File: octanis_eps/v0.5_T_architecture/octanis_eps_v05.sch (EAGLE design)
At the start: 141 parts, among them IC1 OPA2333DGK, Q1 32.768kHz, Q100 BSS123, U1 CSD16327Q3_DQG_8, U10 CSD16327Q3_DQG_8, U100 Value, U11 CSD16327Q3_DQG_8, U2 CSD16327Q3_DQG_8, U3 CSD16327Q3_DQG_8, U4 MSP430G2544, U5 TPS2022D, U6 Value, U7 Value, U8 TPS61232, U9 BQ24650_RVA_16

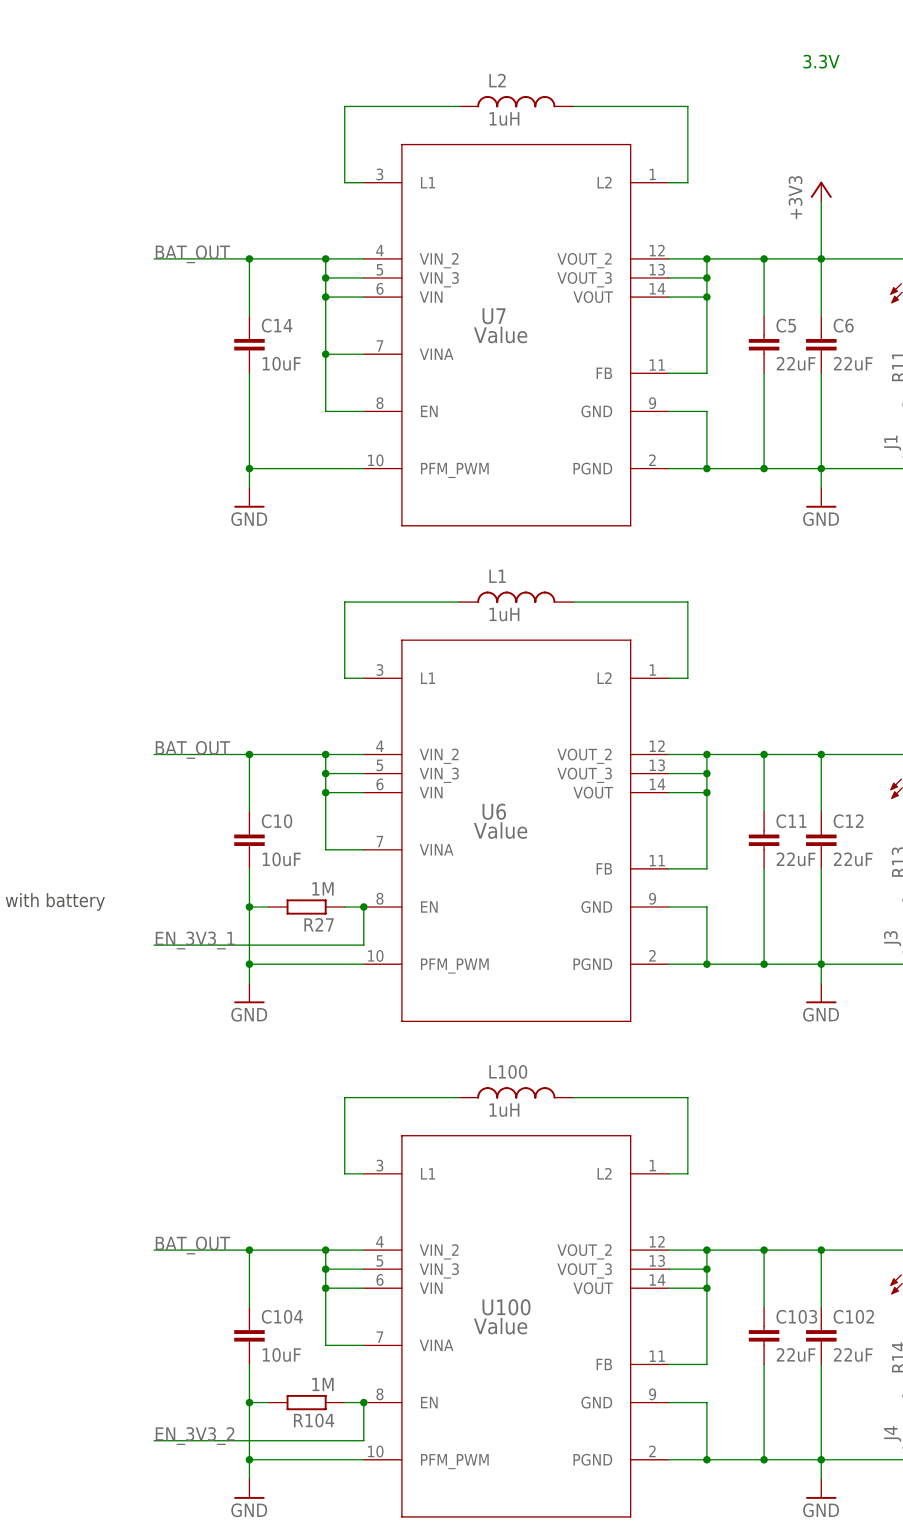
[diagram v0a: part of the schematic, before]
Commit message: replaced 3.3v converters to the BGA component. started moving components to make space on top side
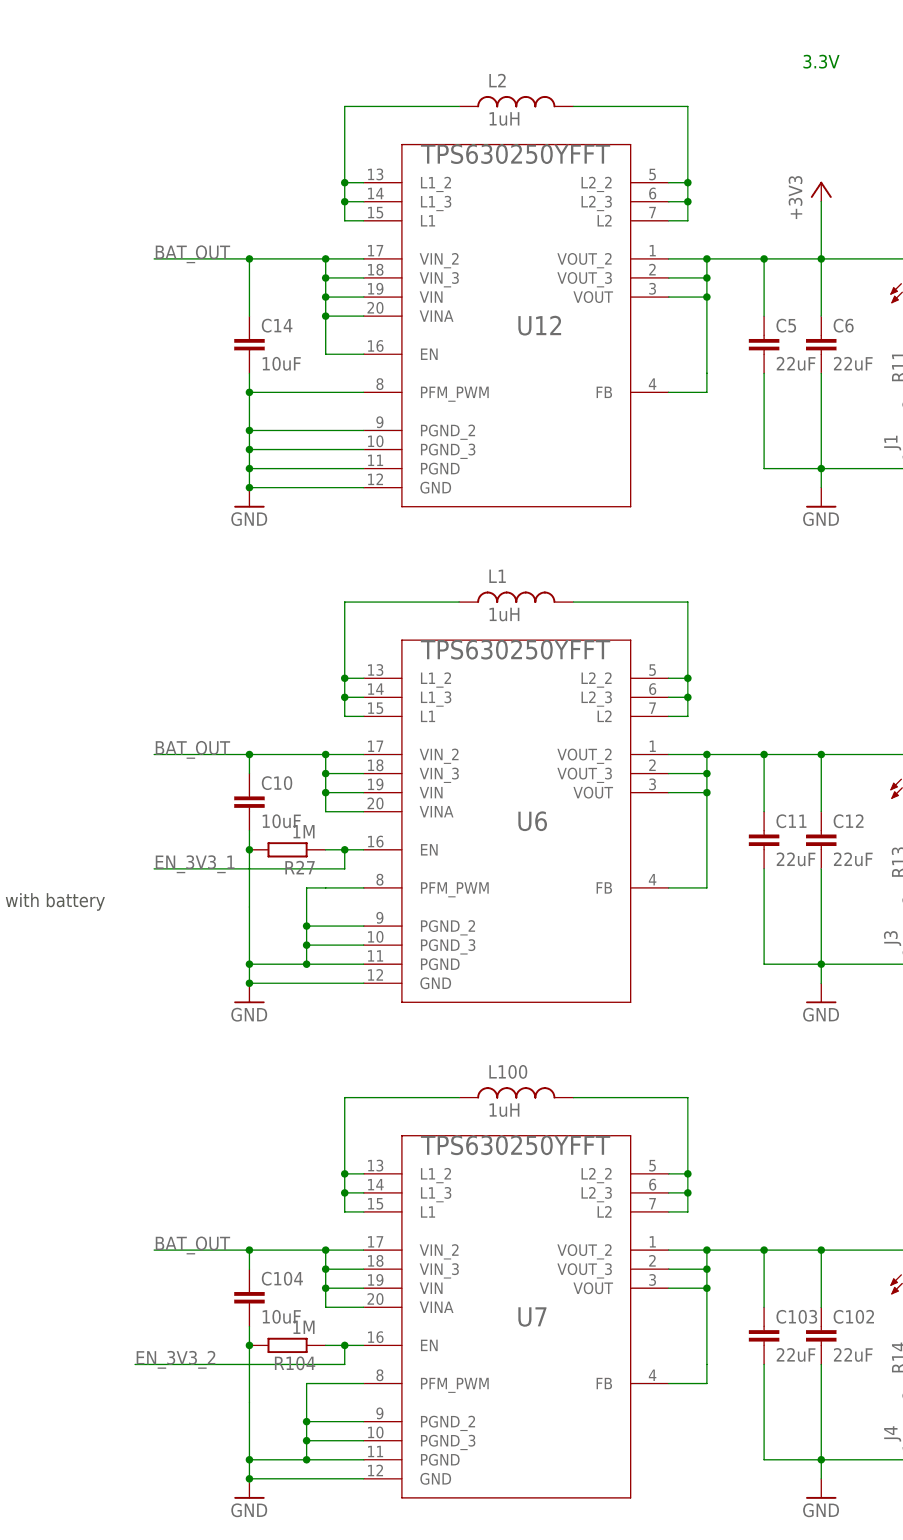
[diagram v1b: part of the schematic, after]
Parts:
- removed U100: Value, octanis_eps_v05:TPS630250RNCR
- added U12: TPS630250YFFT, texasinstruments:TPS630250YFFT
- U6, U7: value Value -> TPS630250YFFT; device octanis_eps_v05:TPS630250RNCR -> texasinstruments:TPS630250YFFT
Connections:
- net +3V3: now also U12.FB, U12.VOUT, U12.VOUT_2, U12.VOUT_3; no longer U7.FB, U7.VOUT, U7.VOUT_2, U7.VOUT_3
- net +3V3_2: now also U7.FB, U7.VOUT, U7.VOUT_2, U7.VOUT_3; no longer U100.FB, U100.VOUT, U100.VOUT_2, U100.VOUT_3
- net BAT_OUT: now also U12.EN, U12.VIN, U12.VINA, U12.VIN_2, U12.VIN_3; no longer U100.VIN, U100.VINA, U100.VIN_2, U100.VIN_3, U7.EN
- net EN_3V3_2: now also U7.EN; no longer U100.EN
- net GND: now also U12.GND, U12.PFM_PWM, U12.PGND, U12.PGND_2, U12.PGND_3, U6.PGND_2, U6.PGND_3, U7.PGND_2, U7.PGND_3; no longer U100.GND, U100.PFM_PWM, U100.PGND
- net N$1: now also U12.L1, U12.L1_2, U12.L1_3; no longer U7.L1
- net N$11: now also U7.L1, U7.L1_2, U7.L1_3; no longer U100.L1
- net N$12: now also U7.L2, U7.L2_2, U7.L2_3; no longer U100.L2
- net N$3: now also U12.L2, U12.L2_2, U12.L2_3; no longer U7.L2
- net N$6: now also U6.L1_2, U6.L1_3
- net N$7: now also U6.L2_2, U6.L2_3
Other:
- moved on the sheet: C10, C104, R104, R27

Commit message: replaced MSP430 for more efficient model. added mosfet circuit braker to schematic
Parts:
- added Q2: BSC340N08NS3G, transistor-power:BSC340N08NS3G
- added R42: dnp, resistor:R-EU_R0603
- added U13: (no value), Seeed-OPL-ic:PMIC-CJ78M05(TO-252)
- added U14: CSD16327Q3_DQG_8, texasinstruments:CSD16327Q3_DQG_8
- added U15: MSP430FR5969, chips:MSP430FR5969
- R35: value 270k -> 100k
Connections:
- removed net N$30: Q1.1, U4.XIN/P2.6
- removed net N$36: Q1.2, U4.XOUT/P2.7
- removed net N$75: JP2.2, U4.TEST/SBWTCK
- removed net N$93: JP2.1, R19.1, U4.RST/NMI/SBWTDIO
- removed net N$99: C3.1, FERRITE.2, U4.AVCC
- new net AGND: C3.2, U15.AVSS
- new net N$10: C3.1, FERRITE.1, U15.AVCC
- new net N$13: JP2.1, R19.1, U15.RST/SBWTDIO
- new net N$15: JP2.2, U15.TEST/SBWTCK
- new net N$16: Q1.1, U15.LFXOUT
- new net N$17: Q1.2, U15.LFXIN
- new net N$9: R42.1, U$1.MODE
- net +3V3: now also FERRITE.2, U15.DVCC; no longer FERRITE.1, U4.DVCC
- net A_EXT1: now also JP1.7, U15.P4.0/A8; no longer JP1.1, U4.P2.4/TA2/A4/VREF+/VEREF+
- net A_EXT2: now also JP1.5, U15.P4.1/A9; no longer JP1.3, U4.P3.0/UCB0STE/UCA0CLK/A5
- net A_EXT3: now also JP1.3, U15.P4.2/A10; no longer JP1.5, U4.P3.6/A6
- net A_EXT4: now also JP1.1, U15.P4.3/A11; no longer JP1.7, U4.P3.7/A7
- net EN_12V: now also U15.P3.5/TB0.4; no longer U4.P1.7/TA2/TDO/TDI
- net EN_3V3_1: now also U15.P4.5; no longer U4.P1.4/SMCLK/TCK
- net EN_3V3_2: now also U15.P4.6; no longer U4.P1.5/TA0/TMS
- net EN_3V3_M: now also U15.P4.4/TB0.5; no longer U4.P1.3/TA2
- net EN_5V: now also U15.P3.6/TB0.5; no longer U4.P1.6/TA1/TDI
- net EN_SC: now also U15.P3.4/TB0.3; no longer U4.P2.5/ROSC
- net GND: now also R42.2, U15.DVSS, U15.VSS_QFN; no longer C3.2, U4.AVSS, U4.DVSS
- net I2C_SCL: now also U15.P1.7/TB0.4/UCB0SOMI/UCB0SCL/TA1.0; no longer U4.P3.2/UCB0SOMI/UCB0SCL
- net I2C_SDA: now also U15.P1.6/TB0.3/UCB0SIMO/UCB0SDA/TA0.0; no longer U4.P3.1/UCB0SIMO/UCB0SDA
- net I_IN: now also U15.P1.1/TA0.2/A1/C1; no longer U4.P2.1/TAINCLK/SMCLK/A1
- net I_OUT: now also U15.P1.0/TA0.1/A0/C0; no longer U4.P2.0/ACLK/A0
- net V_BAT: now also U15.P1.3/TA1.2/UCB0STE/A3/C3; no longer U4.P2.3/TA1/A3/VREF−/VEREF-
- net V_SC: now also U15.P1.2/TA1.1/A2/C2; no longer U4.P2.2/TA0/A2
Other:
- note added: "-> R_ILIM = 100k --> switch current limit = 11.7 A"
- moved on the sheet: C3, C4, C7, FERRITE, JP2, Q1, R19
